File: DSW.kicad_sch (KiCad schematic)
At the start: 0 parts

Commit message: Updates to panel etc.
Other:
- sheet io_board: file io_board/io_board.kicad_sch -> /Users/neil/Projects/euro-modules/DSW/io_board/io_board.kicad_sch
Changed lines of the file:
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@@
       (effects (font (size 1.27 1.27)) (justify left bottom))
     )
-    (property "Sheet file" "io_board/io_board.kicad_sch" (id 1) (at 20.32 65.3546 0)
+    (property "Sheet file" "/Users/neil/Projects/euro-modules/DSW/io_board/io_board.kicad_sch" (id 1) (at 20.32 65.3546 0)
       (effects (font (size 1.27 1.27)) (justify left top))
     )
@@
   )
   (symbol_instances
+    (path "/72a225b7-3740-4caf-9ef5-4c660e16e7b3/e2e6f36d-a4c5-4bbf-b984-5f58c83aac4a"
+      (reference "#FLG0101") (unit 1) (value "~") (footprint "")
+    )
+    (path "/72a225b7-3740-4caf-9ef5-4c660e16e7b3/14e2b2d7-205e-4a1d-accb-ce9c304a7127"
+      (reference "#FLG0102") (unit 1) (value "PWR_FLAG") (footprint "")
+    )
     (path "/fa33938a-7194-4189-9805-2e2648399ea3/330e52fe-aa99-45dc-91ff-e50dc9a6b81e"
       (reference "#PWR01") (unit 1) (value "+12V") (footprint "")
@@
       (reference "#PWR075") (unit 1) (value "+12V") (footprint "")
     )
-    (path "/72a225b7-3740-4caf-9ef5-4c660e16e7b3/94493b84-e929-4463-a482-e9f3aefe2d55"
-      (reference "#PWR076") (unit 1) (value "-12V") (footprint "")
+    (path "/fa33938a-7194-4189-9805-2e2648399ea3/2ca513b1-1df6-4b2e-9000-1b26b3dfa064"
+      (reference "#PWR076") (unit 1) (value "+12V") (footprint "")
     )
     (path "/72a225b7-3740-4caf-9ef5-4c660e16e7b3/01a97d9d-4658-41e4-8112-59251428542f"
@@
       (reference "#PWR080") (unit 1) (value "GND") (footprint "")
     )
-    (path "/72a225b7-3740-4caf-9ef5-4c660e16e7b3/9331c0fb-503b-460a-a5ee-9b485062a5c2"
+    (path "/fa33938a-7194-4189-9805-2e2648399ea3/c9e8ba0e-6d3e-41cf-af76-bd14ac7c94c6"
       (reference "#PWR081") (unit 1) (value "GND") (footprint "")
     )
-    (path "/72a225b7-3740-4caf-9ef5-4c660e16e7b3/1fea594b-6aa3-4b35-8e05-b029ac637c3f"
-      (reference "#PWR082") (unit 1) (value "GND") (footprint "")
+    (path "/fa33938a-7194-4189-9805-2e2648399ea3/9b91d429-0cf5-47cc-b281-42e066fafeb0"
+      (reference "#PWR082") (unit 1) (value "+12V") (footprint "")
     )
     (path "/72a225b7-3740-4caf-9ef5-4c660e16e7b3/a93da5ee-1478-4af1-9df8-9ee2bf4a2f5e"
@@
       (reference "#PWR086") (unit 1) (value "+12V") (footprint "")
     )
-    (path "/72a225b7-3740-4caf-9ef5-4c660e16e7b3/17d1029e-4681-49ef-a2cb-5eb66cdafcab"
+    (path "/fa33938a-7194-4189-9805-2e2648399ea3/7244c532-a541-4af8-9581-aa5e1bbbddb1"
       (reference "#PWR087") (unit 1) (value "GND") (footprint "")
     )
@@
       (reference "#PWR089") (unit 1) (value "GND") (footprint "")
     )
-    (path "/72a225b7-3740-4caf-9ef5-4c660e16e7b3/a870d4c0-c138-4751-8bda-2a7466ded27f"
-      (reference "#PWR090") (unit 1) (value "GND") (footprint "")
-    )
     (path "/72a225b7-3740-4caf-9ef5-4c660e16e7b3/cd20c7e1-f016-4745-8bf6-a32001ecb9cd"
       (reference "#PWR091") (unit 1) (value "-12V") (footprint "")
     )
-    (path "/72a225b7-3740-4caf-9ef5-4c660e16e7b3/ad1295c3-5acc-49c1-ac38-c95e3b6c05a2"
-      (reference "#PWR092") (unit 1) (value "GND") (footprint "")
-    )
-    (path "/72a225b7-3740-4caf-9ef5-4c660e16e7b3/f9b3e1bf-c8c2-4e9e-abec-d7d783ba2564"
-      (reference "#PWR093") (unit 1) (value "GND") (footprint "")
-    )
     (path "/72a225b7-3740-4caf-9ef5-4c660e16e7b3/90c98e93-c769-4589-9cd1-fcfe50594677"
       (reference "#PWR094") (unit 1) (value "+12V") (footprint "")
@@
       (reference "#PWR096") (unit 1) (value "+12V") (footprint "")
     )
-    (path "/72a225b7-3740-4caf-9ef5-4c660e16e7b3/0187c3d0-73b4-4239-8337-903f73b7c7f0"
-      (reference "#PWR097") (unit 1) (value "GND") (footprint "")
-    )
-    (path "/72a225b7-3740-4caf-9ef5-4c660e16e7b3/d0e8cd03-2b53-4359-8039-4ee426071a9e"
-      (reference "#PWR098") (unit 1) (value "GND") (footprint "")
-    )
-    (path "/72a225b7-3740-4caf-9ef5-4c660e16e7b3/1373e820-e5e0-496b-9531-2d2032b601c8"
-      (reference "#PWR099") (unit 1) (value "GND") (footprint "")
-    )
     (path "/72a225b7-3740-4caf-9ef5-4c660e16e7b3/9eeccbb6-7aae-48a7-89fc-3d6e6a7a1ae3"
       (reference "#PWR0100") (unit 1) (value "GND") (footprint "")
@@
       (reference "#PWR0102") (unit 1) (value "GND") (footprint "")
     )
+    (path "/72a225b7-3740-4caf-9ef5-4c660e16e7b3/7a921c78-a310-46d2-a563-852b2fef94c6"
+      (reference "#PWR0103") (unit 1) (value "GND") (footprint "")
+    )
     (path "/72a225b7-3740-4caf-9ef5-4c660e16e7b3/817e6fca-4513-4384-917e-2ca85af7dfdc"
       (reference "#PWR0103") (unit 1) (value "GND") (footprint "")
     )
+    (path "/72a225b7-3740-4caf-9ef5-4c660e16e7b3/fc1c2846-dd66-4867-8313-54979acbb859"
+      (reference "#PWR0104") (unit 1) (value "GND") (footprint "")
+    )
+    (path "/72a225b7-3740-4caf-9ef5-4c660e16e7b3/f686aee0-011d-49d4-b9f1-91a248d4901a"
+      (reference "#PWR0105") (unit 1) (value "GND") (footprint "")
+    )
+    (path "/72a225b7-3740-4caf-9ef5-4c660e16e7b3/1dce6ce4-31d9-4bee-a9d6-9901f6e029ce"
+      (reference "#PWR0106") (unit 1) (value "GND") (footprint "")
+    )
+    (path "/72a225b7-3740-4caf-9ef5-4c660e16e7b3/3af9f9fa-3e94-4340-98e2-3410c5109573"
+      (reference "#PWR0107") (unit 1) (value "GND") (footprint "")
+    )
+    (path "/72a225b7-3740-4caf-9ef5-4c660e16e7b3/6bad5ea4-97d6-45e5-8d3b-344d33374891"
+      (reference "#PWR0108") (unit 1) (value "GND") (footprint "")
+    )
+    (path "/72a225b7-3740-4caf-9ef5-4c660e16e7b3/d3eb4198-b559-406e-ac4e-d34cd4630ba1"
+      (reference "#PWR0109") (unit 1) (value "GND") (footprint "")
+    )
+    (path "/72a225b7-3740-4caf-9ef5-4c660e16e7b3/82840feb-1565-4309-88d9-a3cc42b89ae3"
+      (reference "#PWR0110") (unit 1) (value "GND") (footprint "")
+    )
+    (path "/72a225b7-3740-4caf-9ef5-4c660e16e7b3/248262c4-5b36-450f-b017-166877dbe076"
+      (reference "#PWR0112") (unit 1) (value "-12V") (footprint "")
+    )
+    (path "/72a225b7-3740-4caf-9ef5-4c660e16e7b3/d368aad5-8e1d-4c48-83f3-8abe8e782d28"
+      (reference "#PWR0113") (unit 1) (value "GND1") (footprint "")
+    )
     (path "/fa33938a-7194-4189-9805-2e2648399ea3/e4753580-da38-4fb0-bf28-a1e86ee9b709"
       (reference "C1") (unit 1) (value "10nF") (footprint "Capacitor_THT:C_Disc_D5.0mm_W2.5mm_P2.50mm")
@@
       (reference "R71") (unit 1) (value "1k") (footprint "Resistor_THT:R_Axial_DIN0204_L3.6mm_D1.6mm_P7.62mm_Horizontal")
     )
+    (path "/fa33938a-7194-4189-9805-2e2648399ea3/387a8664-4730-4888-a058-f69d90493bd6"
+      (reference "R72") (unit 1) (value "100k") (footprint "Resistor_THT:R_Axial_DIN0204_L3.6mm_D1.6mm_P7.62mm_Horizontal")
+    )
+    (path "/fa33938a-7194-4189-9805-2e2648399ea3/6ef29dfe-9181-4980-a389-3cb95fbfc0fb"
+      (reference "R73") (unit 1) (value "22k") (footprint "Resistor_THT:R_Axial_DIN0204_L3.6mm_D1.6mm_P7.62mm_Horizontal")
+    )
+    (path "/fa33938a-7194-4189-9805-2e2648399ea3/dcbeef08-0401-40ad-a4d5-065810944955"
+      (reference "R74") (unit 1) (value "100k") (footprint "Resistor_THT:R_Axial_DIN0204_L3.6mm_D1.6mm_P7.62mm_Horizontal")
+    )
+    (path "/fa33938a-7194-4189-9805-2e2648399ea3/27486ba8-ab6e-4f88-9930-826c0e61a758"
+      (reference "R75") (unit 1) (value "22k") (footprint "Resistor_THT:R_Axial_DIN0204_L3.6mm_D1.6mm_P7.62mm_Horizontal")
+    )
     (path "/72a225b7-3740-4caf-9ef5-4c660e16e7b3/50c67057-3d0f-49b5-b902-27cca582d060"

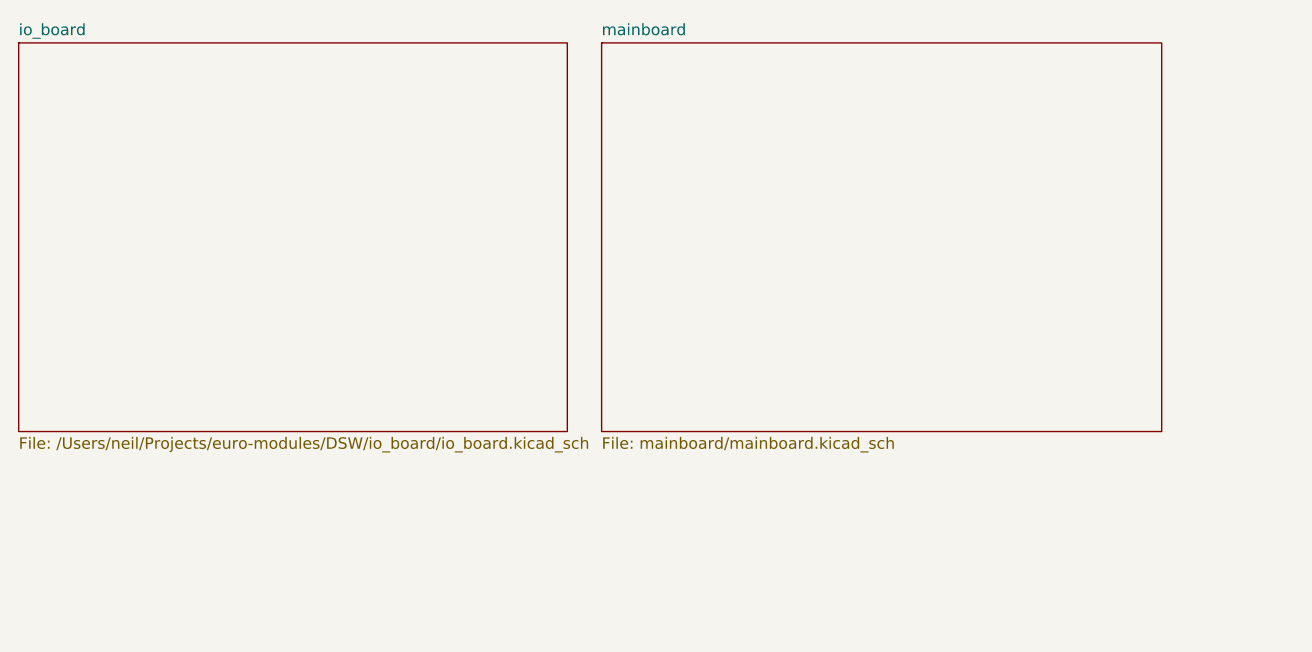
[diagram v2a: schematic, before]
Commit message: Added range switch
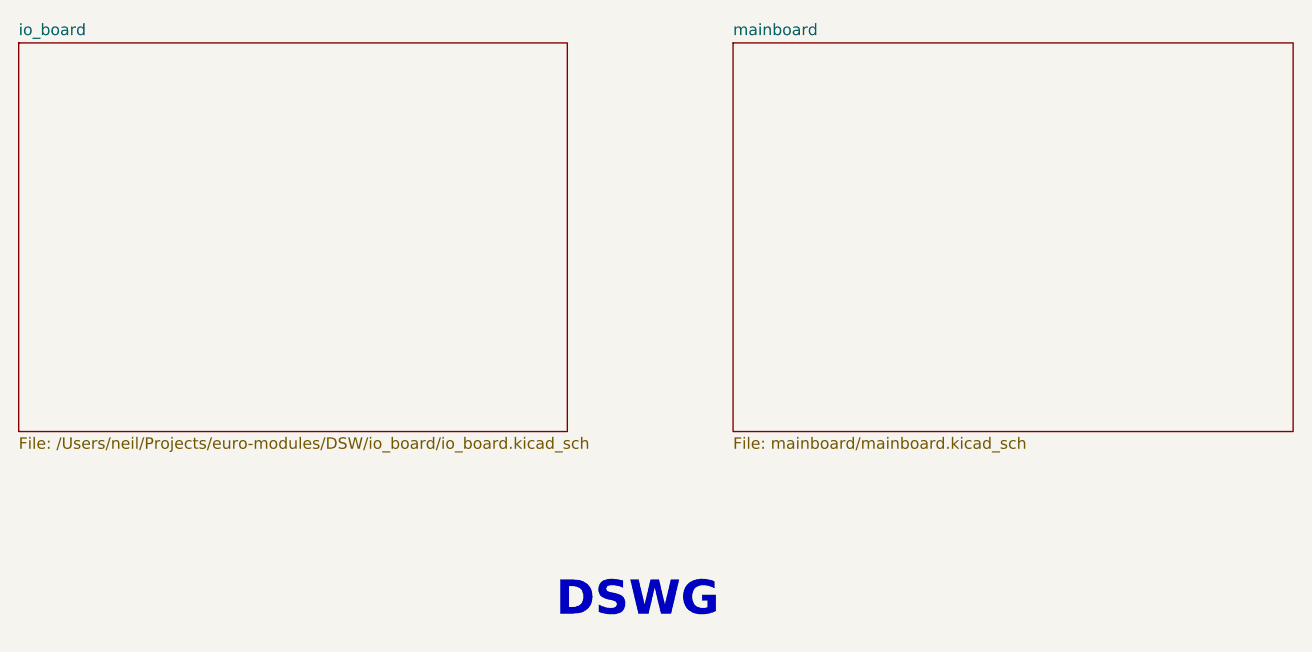
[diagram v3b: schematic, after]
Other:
- note added: "DSWG"
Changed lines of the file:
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@@
 (kicad_sch (version 20211123) (generator eeschema)
-  (paper "A4")
-  (sheet (at 85.09 21.59) (size 62.23 43.18) (fields_autoplaced)
+  (paper "A5")
+  (text "DSWG" (at 80.01 85.725 0)
+    (effects (font (size 3.81 3.81) (thickness 0.762) bold) (justify left bottom))
+  )
+  (sheet (at 99.695 21.59) (size 62.23 43.18) (fields_autoplaced)
     (stroke (width 0.1524) (type solid) (color 0 0 0 0))
     (fill (color 0 0 0 0.0000))
-    (property "Sheet name" "mainboard" (id 0) (at 85.09 20.8784 0)
+    (property "Sheet name" "mainboard" (id 0) (at 99.695 20.8784 0)
       (effects (font (size 1.27 1.27)) (justify left bottom))
     )
-    (property "Sheet file" "mainboard/mainboard.kicad_sch" (id 1) (at 85.09 65.3546 0)
+    (property "Sheet file" "mainboard/mainboard.kicad_sch" (id 1) (at 99.695 65.3546 0)
       (effects (font (size 1.27 1.27)) (justify left top))
     )
@@
       (reference "#PWR076") (unit 1) (value "+12V") (footprint "")
     )
-    (path "/72a225b7-3740-4caf-9ef5-4c660e16e7b3/01a97d9d-4658-41e4-8112-59251428542f"
-      (reference "#PWR077") (unit 1) (value "GND") (footprint "")
-    )
-    (path "/72a225b7-3740-4caf-9ef5-4c660e16e7b3/52822972-38bf-4b2d-ab40-432f15079827"
-      (reference "#PWR078") (unit 1) (value "GND") (footprint "")
-    )
     (path "/72a225b7-3740-4caf-9ef5-4c660e16e7b3/34103d14-3ff6-4888-b7ba-2719ef9085ab"
       (reference "#PWR079") (unit 1) (value "GND") (footprint "")
@@
       (reference "#PWR092") (unit 1) (value "GND") (footprint "")
     )
-    (path "/fa33938a-7194-4189-9805-2e2648399ea3/c6c801eb-a62e-4709-ba8f-cc4ab2962bb0"
-      (reference "#PWR093") (unit 1) (value "GND") (footprint "")
-    )
     (path "/72a225b7-3740-4caf-9ef5-4c660e16e7b3/90c98e93-c769-4589-9cd1-fcfe50594677"
       (reference "#PWR094") (unit 1) (value "+12V") (footprint "")
@@
       (reference "#PWR096") (unit 1) (value "+12V") (footprint "")
     )
-    (path "/fa33938a-7194-4189-9805-2e2648399ea3/5b01a551-5830-4c34-991f-8c4bd9fdd15c"
-      (reference "#PWR097") (unit 1) (value "GND") (footprint "")
-    )
     (path "/72a225b7-3740-4caf-9ef5-4c660e16e7b3/9eeccbb6-7aae-48a7-89fc-3d6e6a7a1ae3"
       (reference "#PWR0100") (unit 1) (value "GND") (footprint "")
@@
       (reference "#PWR0102") (unit 1) (value "GND") (footprint "")
     )
-    (path "/72a225b7-3740-4caf-9ef5-4c660e16e7b3/7a921c78-a310-46d2-a563-852b2fef94c6"
-      (reference "#PWR0103") (unit 1) (value "GND") (footprint "")
-    )
     (path "/72a225b7-3740-4caf-9ef5-4c660e16e7b3/817e6fca-4513-4384-917e-2ca85af7dfdc"
       (reference "#PWR0103") (unit 1) (value "GND") (footprint "")
@@
       (reference "#PWR0110") (unit 1) (value "GND") (footprint "")
     )
+    (path "/fa33938a-7194-4189-9805-2e2648399ea3/7edbd302-d0d6-4d74-80d5-de0cd7cb2744"
+      (reference "#PWR0111") (unit 1) (value "GND") (footprint "")
+    )
     (path "/72a225b7-3740-4caf-9ef5-4c660e16e7b3/248262c4-5b36-450f-b017-166877dbe076"
       (reference "#PWR0112") (unit 1) (value "-12V") (footprint "")
@@
       (reference "#PWR0113") (unit 1) (value "GND1") (footprint "")
     )
+    (path "/fa33938a-7194-4189-9805-2e2648399ea3/2a90a809-3d9a-4601-9b1a-c0e00fe8a14c"
+      (reference "#PWR0114") (unit 1) (value "GND") (footprint "")
+    )
+    (path "/fa33938a-7194-4189-9805-2e2648399ea3/1df5d9fc-bd3f-46f2-956c-fe7cf38b6e49"
+      (reference "#PWR0115") (unit 1) (value "GND") (footprint "")
+    )
+    (path "/fa33938a-7194-4189-9805-2e2648399ea3/c911ef2f-1390-450f-b45b-5d7acaf35583"
+      (reference "#PWR0116") (unit 1) (value "GND") (footprint "")
+    )
+    (path "/72a225b7-3740-4caf-9ef5-4c660e16e7b3/7a921c78-a310-46d2-a563-852b2fef94c6"
+      (reference "#PWR0117") (unit 1) (value "GND") (footprint "")
+    )
     (path "/fa33938a-7194-4189-9805-2e2648399ea3/e4753580-da38-4fb0-bf28-a1e86ee9b709"
       (reference "C1") (unit 1) (value "10nF") (footprint "Capacitor_THT:C_Disc_D5.0mm_W2.5mm_P2.50mm")
@@
       (reference "C6") (unit 1) (value "10nF") (footprint "Capacitor_THT:C_Disc_D5.0mm_W2.5mm_P2.50mm")
     )
-    (path "/72a225b7-3740-4caf-9ef5-4c660e16e7b3/7055b123-b9dd-42d6-8399-8f8f2c90fb10"
-      (reference "C7") (unit 1) (value "10nF") (footprint "Capacitor_THT:C_Disc_D5.0mm_W2.5mm_P2.50mm")
-    )
-    (path "/72a225b7-3740-4caf-9ef5-4c660e16e7b3/1deb2202-bcf8-45d2-8311-d5516c135674"
-      (reference "C8") (unit 1) (value "10nf") (footprint "Capacitor_THT:C_Disc_D5.0mm_W2.5mm_P2.50mm")
+    (path "/fa33938a-7194-4189-9805-2e2648399ea3/7c73c380-6a67-42b6-afef-7a004a73a550"
+      (reference "C7") (unit 1) (value "1nF") (footprint "Capacitor_THT:C_Disc_D5.0mm_W2.5mm_P2.50mm")
+    )
+    (path "/fa33938a-7194-4189-9805-2e2648399ea3/d4899075-c568-4ba8-8af4-93abffc9a38e"
+      (reference "C8") (unit 1) (value "100nF") (footprint "Capacitor_THT:C_Disc_D5.0mm_W2.5mm_P2.50mm")
     )
     (path "/72a225b7-3740-4caf-9ef5-4c660e16e7b3/cfdf7467-9ce0-49f0-b5bd-de77a94a2388"
@@
       (reference "C15") (unit 1) (value "100nF") (footprint "Capacitor_THT:C_Disc_D5.0mm_W2.5mm_P2.50mm")
     )
+    (path "/fa33938a-7194-4189-9805-2e2648399ea3/190294cd-6b0f-4233-ad57-e3fd008a000b"
+      (reference "C16") (unit 1) (value "1nF") (footprint "Capacitor_THT:C_Disc_D5.0mm_W2.5mm_P2.50mm")
+    )
+    (path "/fa33938a-7194-4189-9805-2e2648399ea3/4e8994f7-71ec-452f-92f8-63b4a2e20a41"
+      (reference "C17") (unit 1) (value "100nF") (footprint "Capacitor_THT:C_Disc_D5.0mm_W2.5mm_P2.50mm")
+    )
     (path "/fa33938a-7194-4189-9805-2e2648399ea3/60582e37-12cd-424a-bb26-9419cc055411"
       (reference "CVR1") (unit 1) (value "10k") (footprint "winterbloom:Potentiometer_Alpha_R0904N")
@@
       (reference "D14") (unit 1) (value "BAT42") (footprint "Diode_THT:D_DO-35_SOD27_P7.62mm_Horizontal")
     )
-    (path "/fa33938a-7194-4189-9805-2e2648399ea3/b4e0d83a-1e44-4055-b69b-34a66bed64e8"
-      (reference "D15") (unit 1) (value "BAT42") (footprint "Diode_THT:D_DO-35_SOD27_P7.62mm_Horizontal")
-    )
-    (path "/fa33938a-7194-4189-9805-2e2648399ea3/61cd796f-f9d1-45f6-922e-b46b67f716a1"
-      (reference "D16") (unit 1) (value "BAT42") (footprint "Diode_THT:D_DO-35_SOD27_P7.62mm_Horizontal")
-    )
     (path "/fa33938a-7194-4189-9805-2e2648399ea3/a2167960-f9c9-4609-b610-0da799bcc1d1"
       (reference "FREQ1") (unit 1) (value "10k") (footprint "winterbloom:Potentiometer_Alpha_R0904N")
@@
       (reference "SW1") (unit 1) (value "SW_SPDT") (footprint "winterbloom:Miniature_Switch_SPDT_2.54MM")
     )
+    (path "/fa33938a-7194-4189-9805-2e2648399ea3/fdd4009f-912f-4aa5-91fe-ec8d40513670"
+      (reference "SW2") (unit 1) (value "SW_SPDT") (footprint "winterbloom:Miniature_Switch_SPDT_2.54MM")
+    )
+    (path "/fa33938a-7194-4189-9805-2e2648399ea3/617a38c8-4ba5-4eeb-a5b5-2a14bda91da6"
+      (reference "SW3") (unit 1) (value "SW_SPDT") (footprint "winterbloom:Miniature_Switch_SPDT_2.54MM")
+    )
     (path "/fa33938a-7194-4189-9805-2e2648399ea3/ef136bc0-ff96-458a-8946-0141f412bcf8"
